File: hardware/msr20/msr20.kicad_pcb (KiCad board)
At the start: 2 copper layers, 120 x 100 mm, 56 parts, among them J1 Conn_Coaxial, U1 NCP1117-12_SOT223, U11 BGA616, U13 ADE-1+, U14 AD7478, U15 MC1350, U16 LTC455-FU, U4 RF-BPF, U5 Pico, U6 74LS163, U7 CD74HC4046, U8 NCP1117-3.3_SOT223, U9 NCP1117-5.0_SOT223

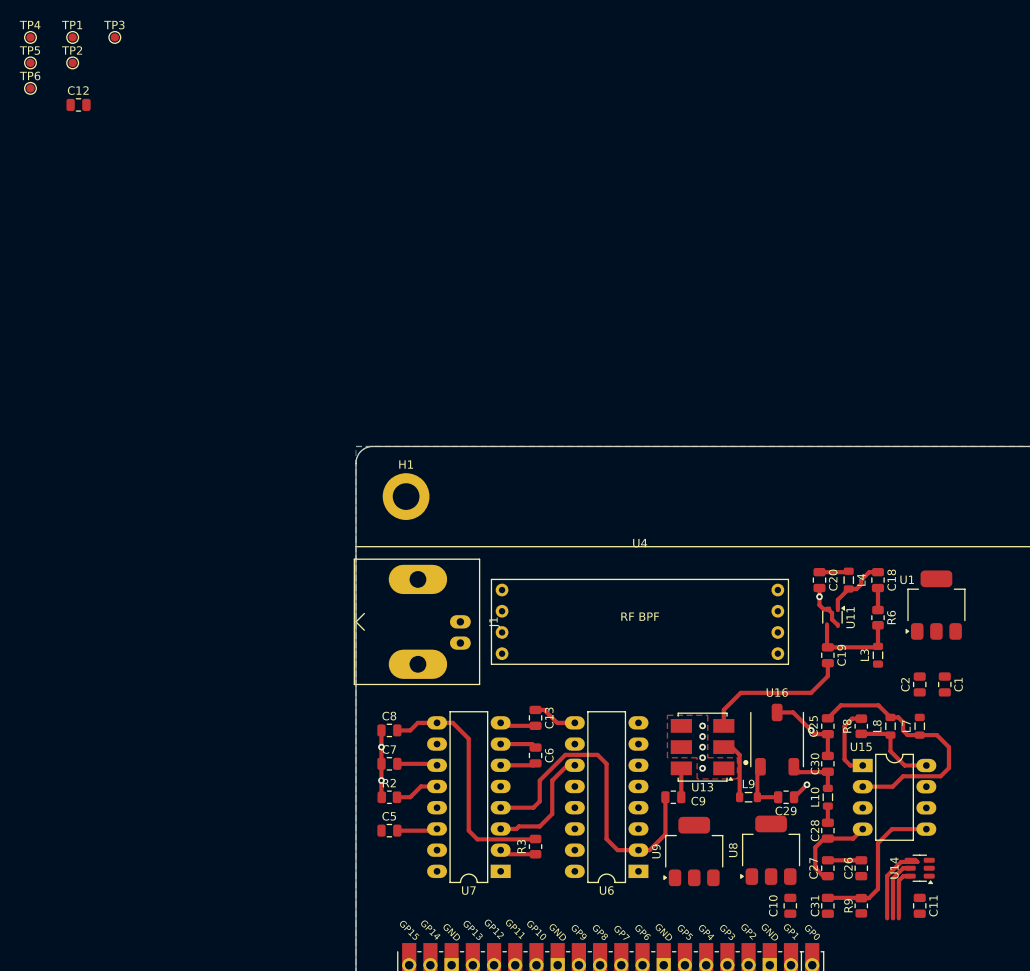
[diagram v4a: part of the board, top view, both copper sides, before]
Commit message: power and ground routing
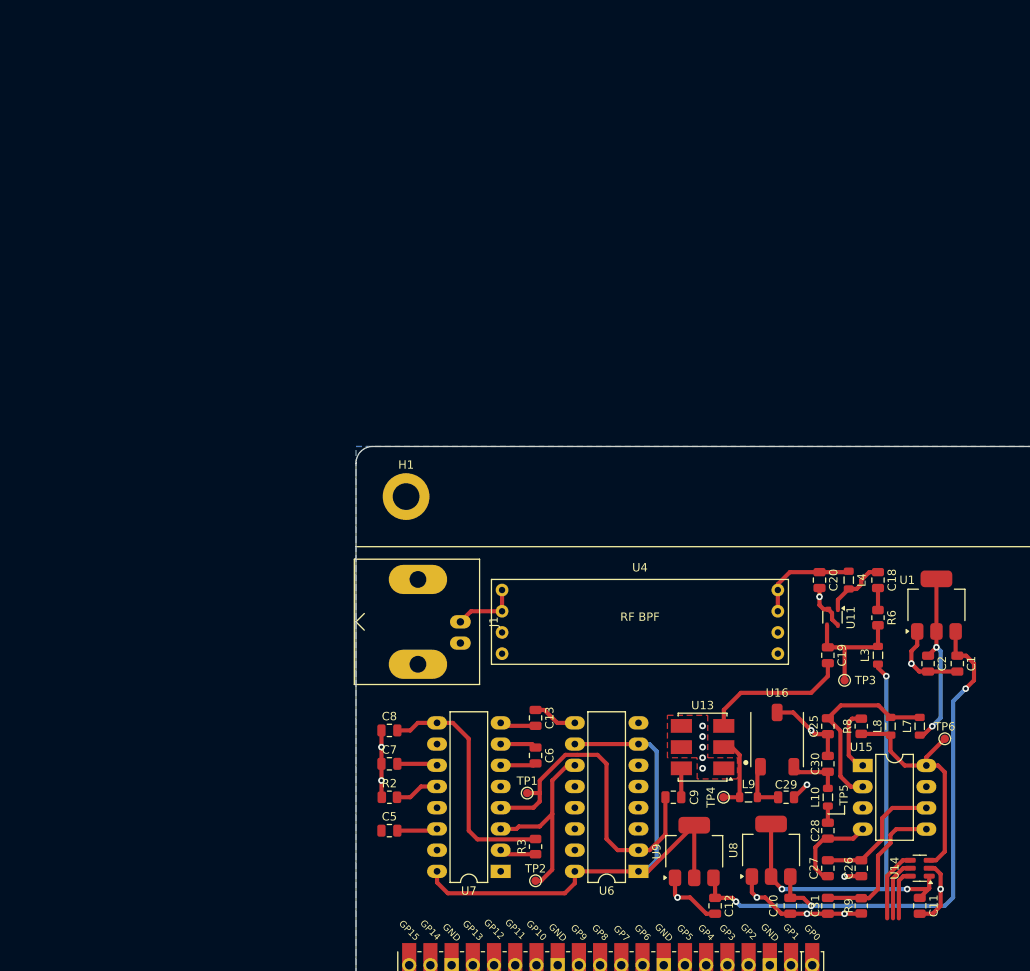
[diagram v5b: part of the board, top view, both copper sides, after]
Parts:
- removed TP5: TestPoint, TestPoint:TestPoint_Pad_D1.0mm
- moved TP6 134.3 mm to (110.5, 85.0)
- moved TP4 123.1 mm to (84.0, 92.0)
- moved C12 122.5 mm to (83.0, 105.0), turned to -90 degrees
- moved TP3 116.4 mm to (98.5, 78.0)
- moved TP2 112.5 mm to (61.5, 102.0)
- moved TP1 105.6 mm to (60.5, 91.5)
- moved C1 2.92 mm to (112.0, 76.0)
- moved C2 2.69 mm to (108.5, 76.0), turned to -90 degrees
- turned L7 to -90 degrees
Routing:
- net VIN: track 0.00 -> 71.6 mm, vias 0 -> 3
- net +5V: track 5.34 -> 74.4 mm
- net +3.3V: track 0.00 -> 56.4 mm, vias 0 -> 3
- net GND: track 29.9 -> 74.2 mm, vias 10 -> 17
- net +12V: track 0.00 -> 21.7 mm, vias 0 -> 2
- net Net-(U14-VIN): track 10.5 -> 28.9 mm
- net Net-(U15-IN+): track 4.00 -> 15.9 mm
- net Net-(U6-Qd): track 14.4 -> 23.6 mm
- net Net-(C20-Pad1): track 3.55 -> 12.4 mm
- net Net-(U15-VCC): track 31.6 -> 23.0 mm
- net Net-(J1-In): track 0.00 -> 8.06 mm
- net Net-(U11-OUT): track 11.3 -> 15.2 mm
- net /IF Stage/INPUT: track 7.35 -> 9.29 mm
- net ADC-SCK: track 10.3 -> 8.62 mm
- net Net-(U6-CLK): track 39.0 -> 40.5 mm
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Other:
- board text added: "TP5"
